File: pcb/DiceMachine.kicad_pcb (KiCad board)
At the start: 2 copper layers, 60 x 40 mm, 12 parts, among them J1 Conn_01x02, J2 Conn_01x02, J3 Conn_01x02, U1 arduino_mini

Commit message: created PCB gerber files
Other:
- board text added: "DiceMachine v1.0"
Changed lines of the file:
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@@
     (links 23)
     (no_connects 0)
-    (area 100.814999 68.614999 160.965001 108.765001)
+    (area 100.814999 67.959499 178.305002 111.920501)
     (thickness 1.6)
-    (drawings 5)
+    (drawings 6)
     (tracks 46)
     (zones 0)
@@
     (visible_elements 7FFFFFFF)
     (pcbplotparams
-      (layerselection 0x00030_80000001)
-      (usegerberextensions false)
+      (layerselection 0x010f0_80000001)
+      (usegerberextensions true)
       (excludeedgelayer true)
       (linewidth 0.100000)
@@
       (outputformat 1)
       (mirror false)
-      (drillshape 1)
+      (drillshape 0)
       (scaleselection 1)
-      (outputdirectory ""))
+      (outputdirectory DiceMachine_gerber/))
   )
   (net 0 "")
@@
     (descr "Through hole pin header")
     (tags "pin header")
-    (fp_text reference NOK1 (at 0 -5.1 180) (layer F.SilkS)
+    (fp_text reference NOK1 (at 2.55 17.13 270) (layer F.SilkS)
       (effects (font (size 1 1) (thickness 0.15)))
     )
@@
       (net 5 "Net-(J3-Pad1)"))
   )
+  (gr_text "DiceMachine v1.0" (at 157.92 96.73 90) (layer F.SilkS)
+    (effects (font (size 1.5 1.5) (thickness 0.3)))
+  )
   (gr_text "+ -" (at 108.09 75.55 180) (layer F.SilkS)

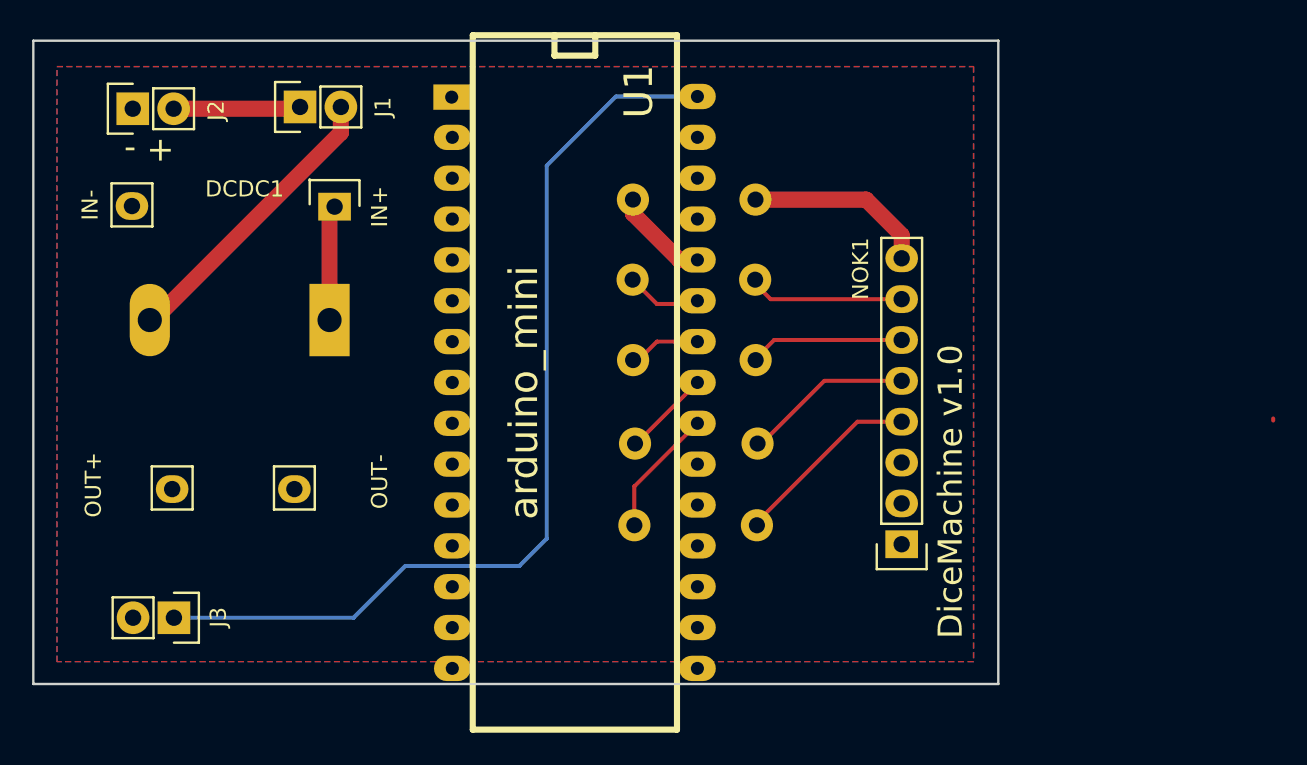
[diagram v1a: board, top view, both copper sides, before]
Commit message: added level shifter to PCB
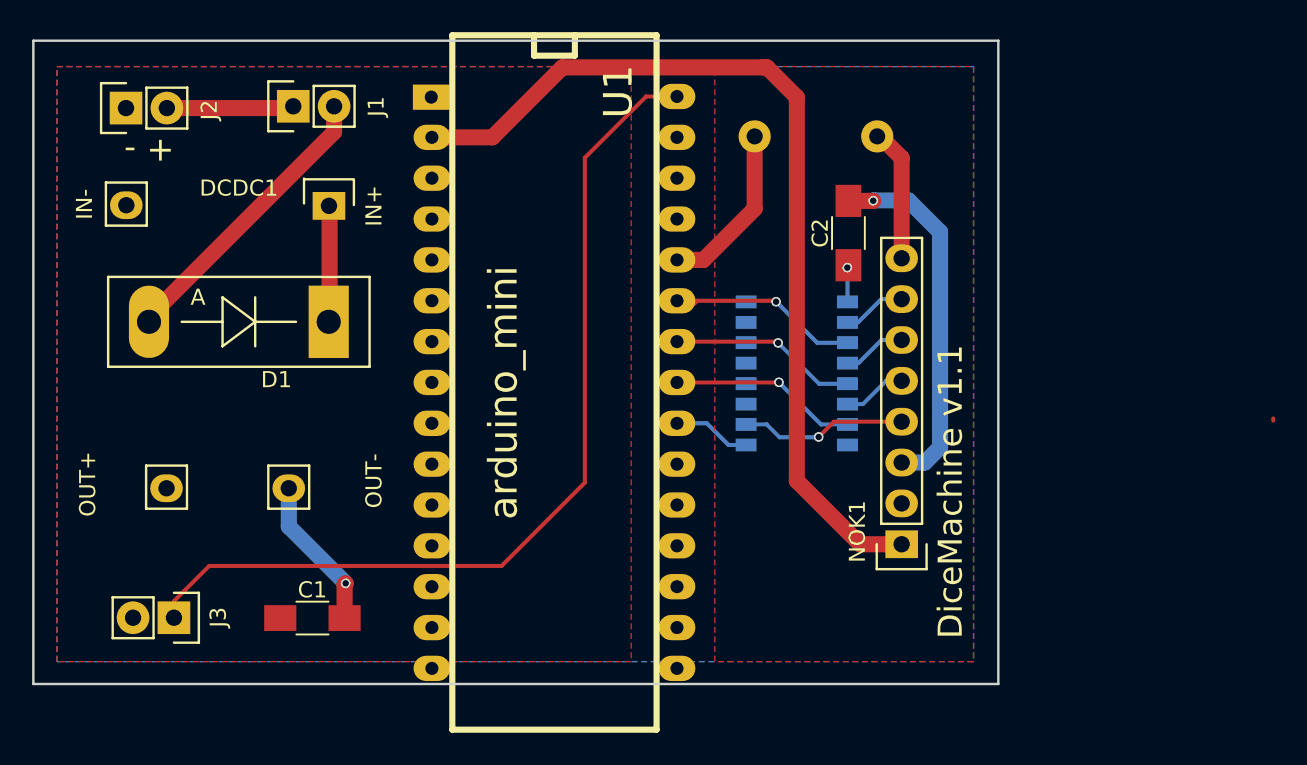
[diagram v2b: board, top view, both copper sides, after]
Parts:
- removed R2, R3, R4, R5: 10k, Resistors_ThroughHole:Resistor_Horizontal_RM7mm
- added C1: C, Capacitors_SMD:C_1206_HandSoldering, F.Cu at (118.2, 104.6)
- added C2: C, Capacitors_SMD:C_1206_HandSoldering, F.Cu at (151.6, 80.7)
- added LS1: LevelShifter_74HC4050D, Housings_SSOP:SOP-16_4.4x10.4mm_Pitch1.27mm, B.Cu at (148.4, 89.4)
- D1: moved to F.Cu
- moved R1 8.53 mm to (153.4, 74.6)
- moved U1 1.27 mm to (133.3, 91.2)
- moved J1 0.42 mm to (117.0, 72.8)
- moved J2 0.42 mm to (106.7, 72.9)
- moved DCDC1 0.35 mm to (113.0, 99.4)
- moved D1 0.12 mm to (119.2, 86.2)
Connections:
- NOK1 pad 1: +5V -> +3V3
- U1 pad 2: Net-(U1-Pad2) -> +3V3
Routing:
- net +3V3: track 0.00 -> 59.6 mm, vias 0 -> 1
- net GND: track 0.00 -> 32.3 mm, vias 0 -> 2
- net Net-(LS1-Pad3): track 4.74 -> 12.0 mm, vias 0 -> 1
- net Net-(LS1-Pad5): track 4.48 -> 11.7 mm, vias 0 -> 1
- net Net-(LS1-Pad6): track 10.6 -> 3.97 mm
- net Net-(LS1-Pad7): track 5.45 -> 11.7 mm, vias 0 -> 1
- net Net-(LS1-Pad4): track 9.97 -> 3.97 mm
- net Net-(LS1-Pad2): track 9.76 -> 3.97 mm
- net Net-(R1-Pad2): track 6.07 -> 10.6 mm
- net Net-(NOK1-Pad8): track 11.4 -> 8.32 mm
- net Net-(LS1-Pad9): track 7.96 -> 4.86 mm
- net Net-(J3-Pad1): track 59.6 -> 57.1 mm
- net Net-(LS1-Pad10): track 12.5 -> 10.5 mm, vias 0 -> 1
- added copper zone on F.Cu, net +3V3
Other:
- board text added: "DiceMachine v1.1"
- board text removed: "DiceMachine v1.0"
